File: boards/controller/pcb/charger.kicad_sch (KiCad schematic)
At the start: 41 parts, among them J5 Conn_01x02_Socket, J6 Conn_01x04_Socket

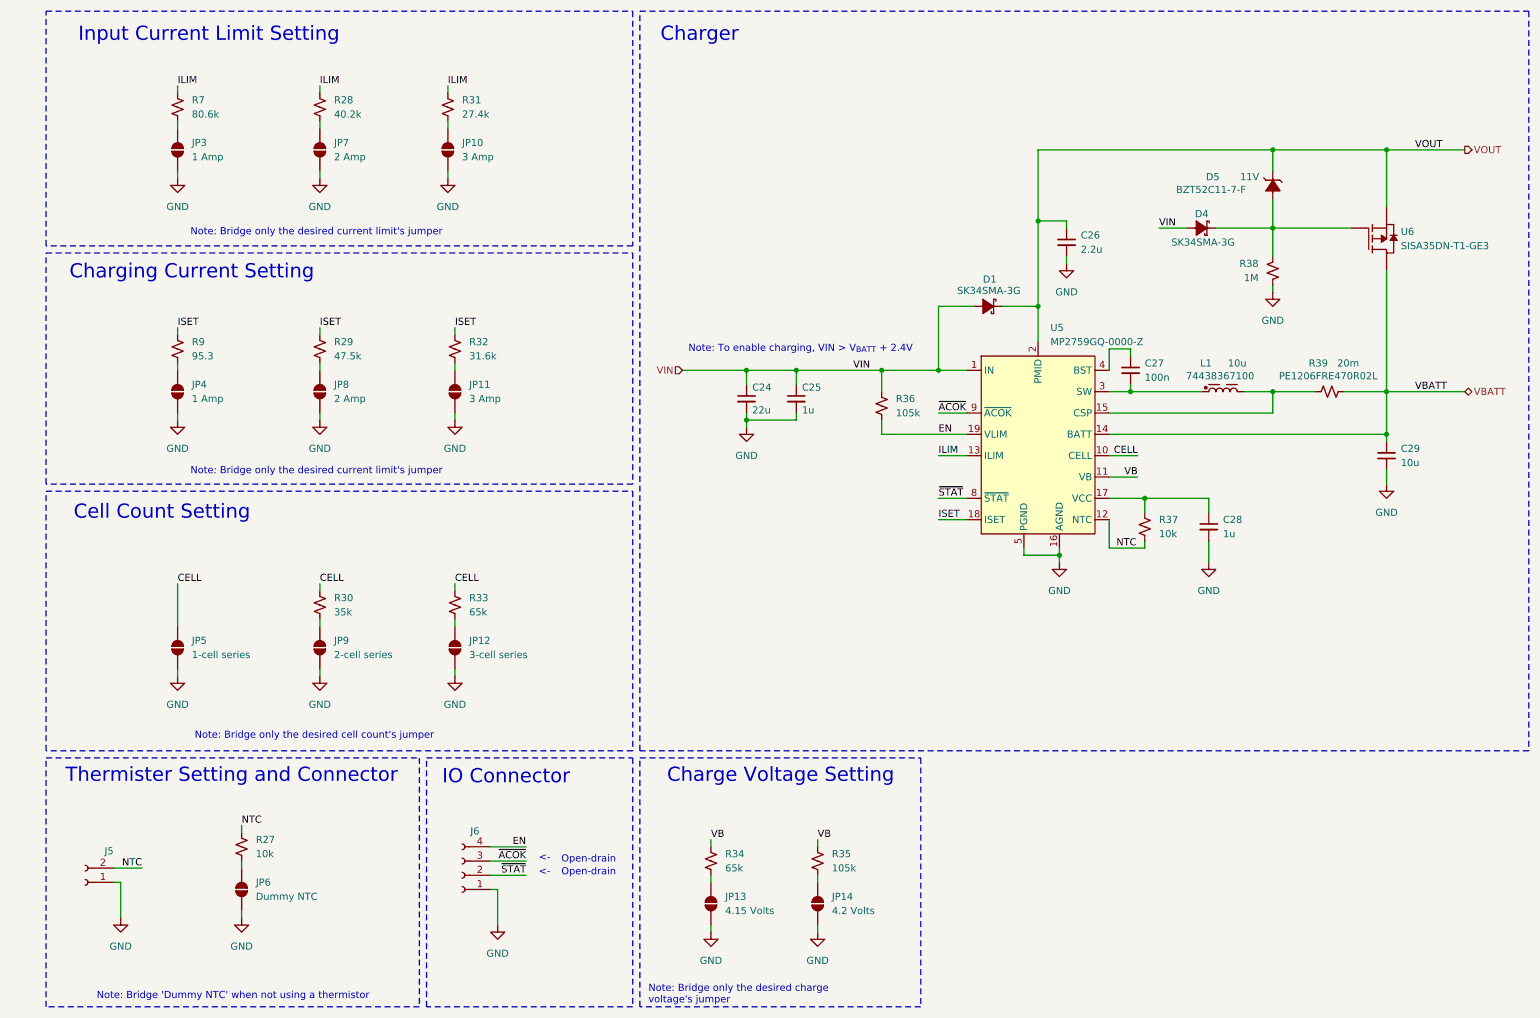
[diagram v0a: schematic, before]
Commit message: controller: Update PCB
Signed-off-by: Nicholas Loehrke <nicholasnloehrke@gmail.com>
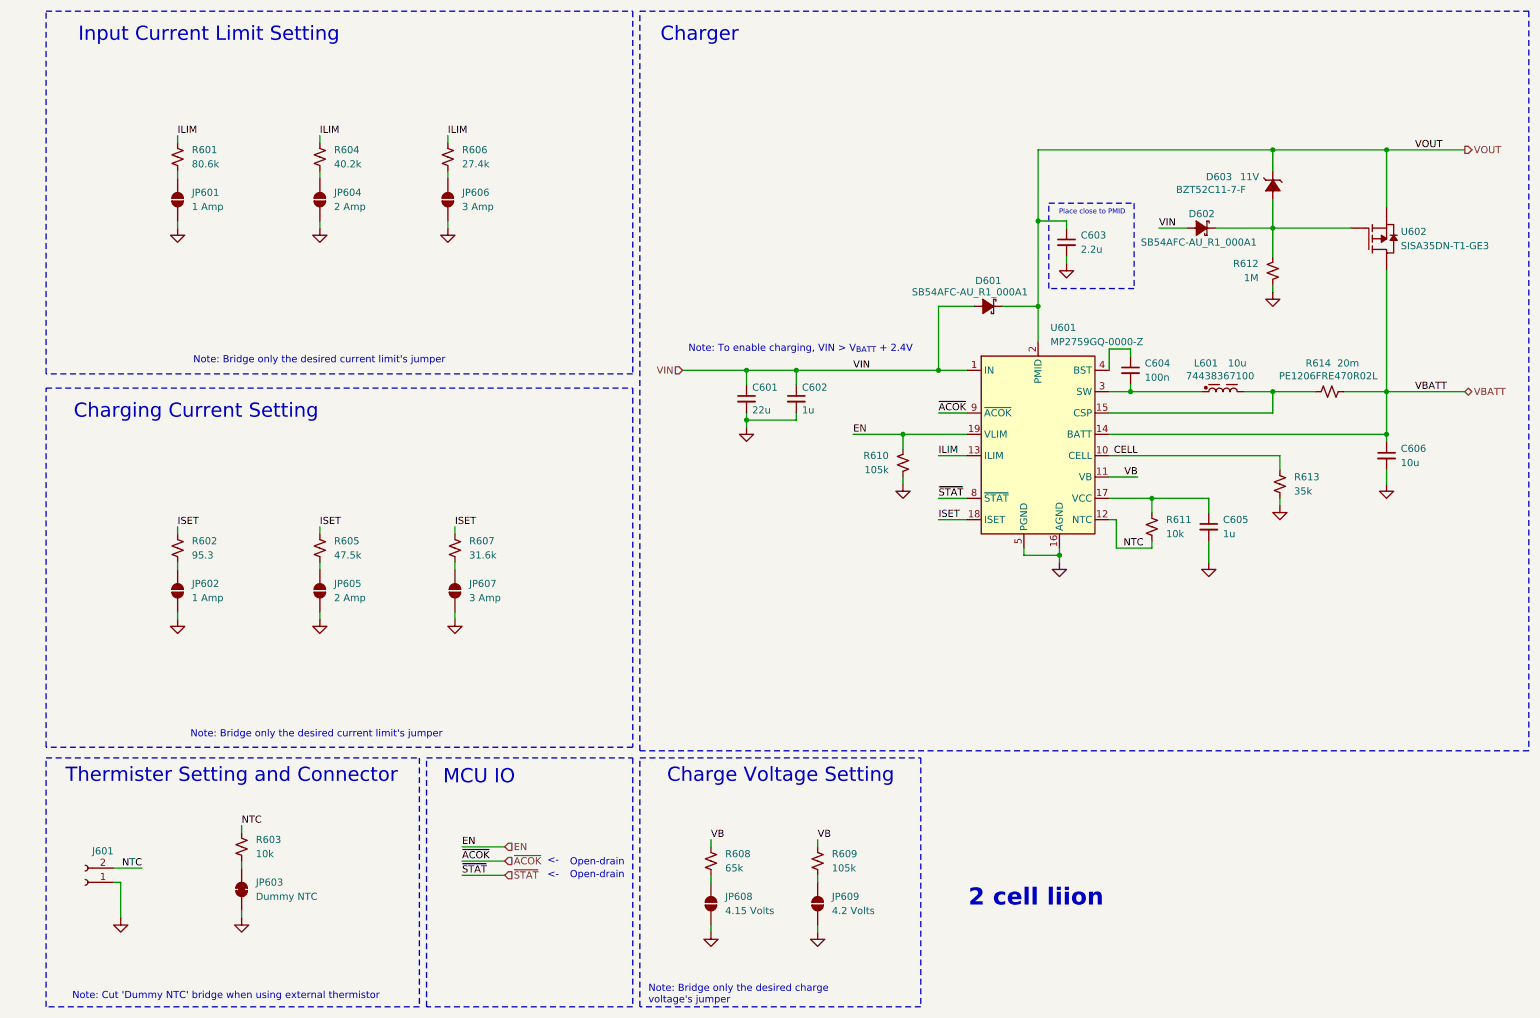
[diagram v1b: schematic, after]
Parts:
- removed D1, D4: ~, SK34SMA-3G:SK34SMA-3G, symbol SK34SMA-3G:SK34SMA-3G
- removed J6: Conn_01x04_Socket, Connector_JST:JST_XH_B4B-XH-A_1x04_P2.50mm_Vertical, symbol Connector:Conn_01x04_Socket
- removed JP12: 3-cell series, Jumper:SolderJumper-2_P1.3mm_Open_RoundedPad1.0x1.5mm, symbol Jumper:SolderJumper_2_Open
- removed JP5: 1-cell series, Jumper:SolderJumper-2_P1.3mm_Open_RoundedPad1.0x1.5mm, symbol Jumper:SolderJumper_2_Open
- removed JP6: Dummy NTC, Jumper:SolderJumper-2_P1.3mm_Open_RoundedPad1.0x1.5mm, symbol Jumper:SolderJumper_2_Open
- removed JP9: 2-cell series, Jumper:SolderJumper-2_P1.3mm_Open_RoundedPad1.0x1.5mm, symbol Jumper:SolderJumper_2_Open
- removed R30: 35k, Resistor_SMD:R_0603_1608Metric, symbol Device:R_Small_US
- removed R33: 65k, Resistor_SMD:R_0603_1608Metric, symbol Device:R_Small_US
- removed R36: 105k, Resistor_SMD:R_0603_1608Metric, symbol Device:R_Small_US
- added D601, D602: SB54AFC-AU_R1_000A1, DIODE_SB54AFC-AU_R1_000A1_PNJ, symbol SB54AFC-AU_R1_000A1:SB54AFC-AU_R1_000A1
- added JP603: Dummy NTC, symbol Jumper:SolderJumper_2_Bridged
- added R610: 105k, Resistor_SMD:R_0603_1608Metric, symbol Device:R_Small_US
- added R613: 35k, Resistor_SMD:R_0603_1608Metric, symbol Device:R_Small_US
- renumbered C24 to C601, C25 to C602, C26 to C603, C27 to C604, C28 to C605, C29 to C606, D5 to D603, J5 to J601, JP3 to JP601, JP4 to JP602, JP7 to JP604, JP8 to JP605, JP10 to JP606, JP11 to JP607, JP13 to JP608, JP14 to JP609, L1 to L601, R7 to R601, R9 to R602, R27 to R603, R28 to R604, R29 to R605, R31 to R606, R32 to R607, R34 to R608, R35 to R609, R37 to R611, R38 to R612, R39 to R614, U5 to U601, U6 to U602
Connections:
- net CELL: now also R613.1
- net EN: now also R610.1
- net GND: now also JP603.1 (A), R610.2, R613.2
- net VIN: now also D601.2, D602.2
- net VOUT: now also D601.1
- net at D603.2, R612.1, U602.4: now also D602.1
- net at R603.2: now also JP603.2 (B)
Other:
- note added: "2 cell liion"
- note added: "MCU IO"
- note added: "Note: Cut 'Dummy NTC' bridge when using external thermistor"
- note added: "Place close to PMID"
- note removed: "Cell Count Setting"
- note removed: "IO Connector"
- note removed: "Note: Bridge 'Dummy NTC' when not using a thermistor"
- note removed: "Note: Bridge only the desired cell count's jumper"
- moved on the sheet: JP601, JP602, JP604, JP605, JP606, JP607, R601, R602, R604, R605, R606, R607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
